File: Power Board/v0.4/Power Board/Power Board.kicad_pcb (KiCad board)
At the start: 4 copper layers, 70 x 80 mm, 89 parts, among them J1 Battery In, J2 JST B2PS-VH, J3 JST B2PS-VH, J4 JST B2PS-VH, J5 JST B2PS-VH, J6 JST B2PS-VH, J7 JST B2PS-VH, J9 Raspberry Pi, Q1 SI5504BDC, SW1 SW_Push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

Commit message: Final Layout
Just need silk screen cleanup
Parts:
- moved F4 13.9 mm to (138.2, 57.5)
- moved F5 13.9 mm to (138.2, 71.5)
- moved L5 9.89 mm to (139.5, 76.2), turned to 270 degrees
- moved L4 9.64 mm to (139.5, 62.2), turned to 270 degrees
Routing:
- net GND: vias 83 -> 272
- net Net-(F5-Pad1): vias 0 -> 8
- net Net-(F4-Pad1): vias 0 -> 8
- net Net-(C1-Pad1): vias 0 -> 1
- added copper zone on B.Cu, net Net-(F4-Pad1)
- added copper zone on F.Cu, net Net-(F4-Pad1)
- added copper zone on B.Cu, net Net-(F5-Pad1)
- added copper zone on F.Cu, net Net-(F5-Pad1)
- added copper zone on B.Cu, net Net-(J5-Pad1)
- added copper zone on B.Cu, net Net-(J6-Pad1)

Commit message: Add 3D models for some components.
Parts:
- J1: footprint Connector_JST:JST_VH_B3PS-VH_1x03_P3.96mm_Horizontal -> Power_Board:JST_VH_B3PS-VH_1x03_P3.96mm_Horizontal
- J2, J3, J4, J5, J6, J7: footprint Connector_JST:JST_VH_B2PS-VH_1x02_P3.96mm_Horizontal -> Power_Board:JST_VH_B2PS-VH_1x02_P3.96mm_Horizontal

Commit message: Add 3D models for more components.
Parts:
- F1, F2, F3, F4, F5, F6: footprint Fuse:Fuse_1206_3216Metric -> Power_Board:Fuse_1206_3216Metric
- U2: footprint Package_DFN_QFN:VQFN-16-1EP_3x3mm_P0.5mm_EP1.68x1.68mm_ThermalVias -> Power_Board:VQFN-16-1EP_3x3mm_P0.5mm_EP1.68x1.68mm_ThermalVias

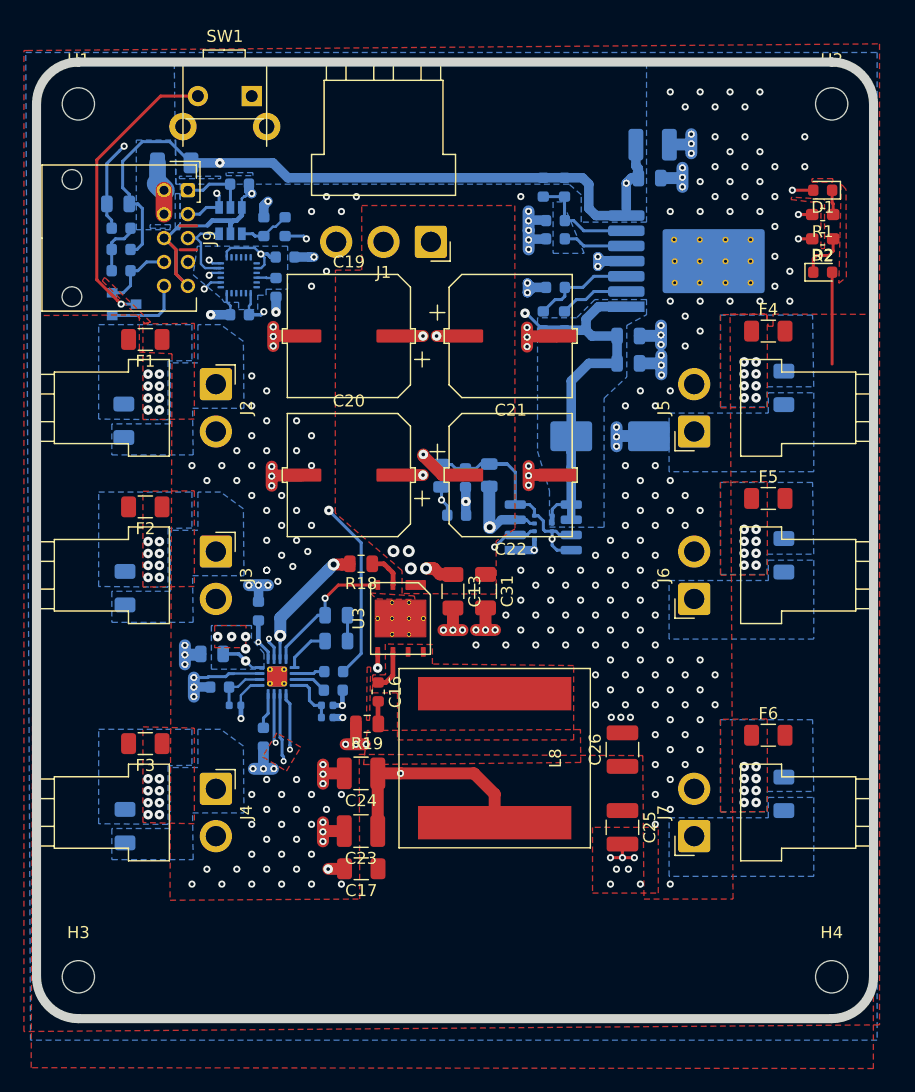
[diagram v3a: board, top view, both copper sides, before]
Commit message: Clean up silkscreen, add logo artwork.
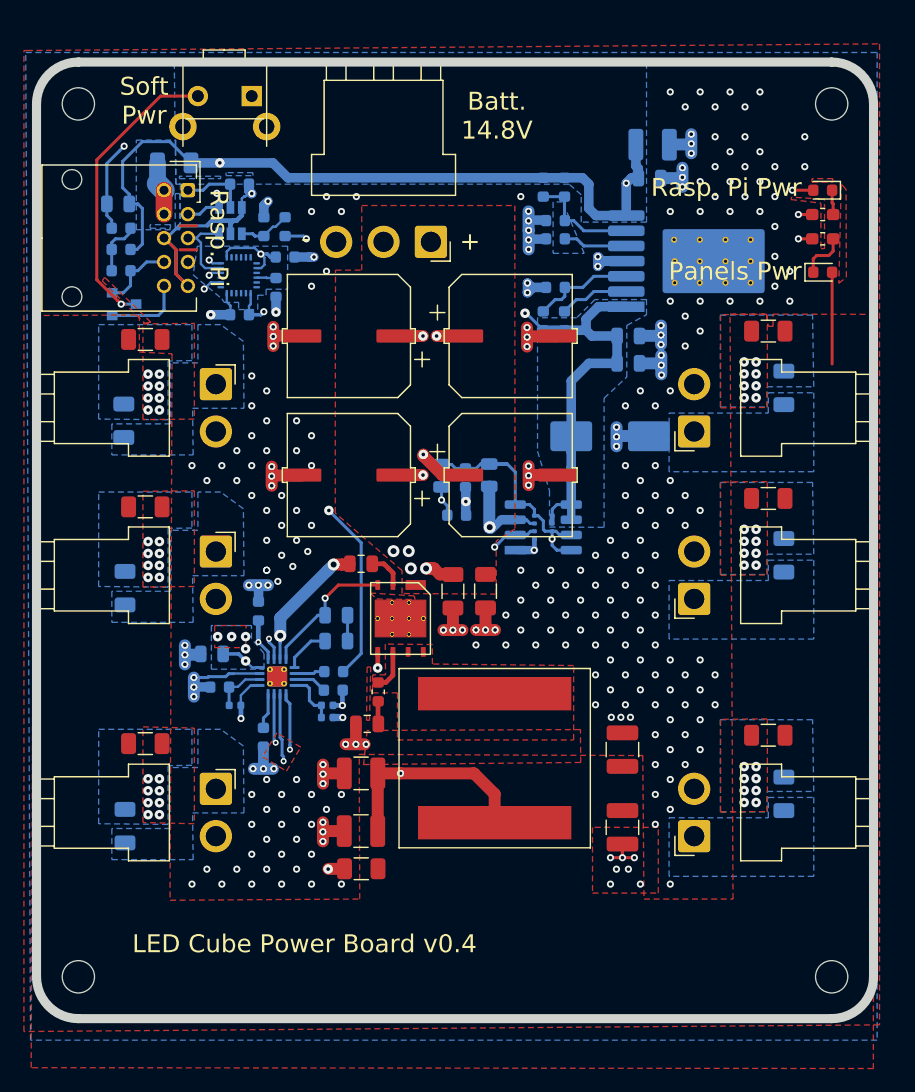
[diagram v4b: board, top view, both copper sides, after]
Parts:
- added G***: LOGO, Power_Board:Logo Silkscreen, B.Cu at (117.5, 93.2)
- added G***: LOGO, Power_Board:Logo Solder Mask, B.Cu at (117.5, 93.2)
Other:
- board text added: "+"
- board text added: "-"
- board text added: "Batt. 14.8V"
- board text added: "LED Cube Power Board v0.4"
- board text added: "Panels Pwr"
- board text added: "Rasp. Pi"
- board text added: "Rasp. Pi Pwr"
- board text added: "Soft Pwr"
